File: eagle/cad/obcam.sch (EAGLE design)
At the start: 15 parts, among them IC1 NJM2391, IC2 TJ8S06M3L

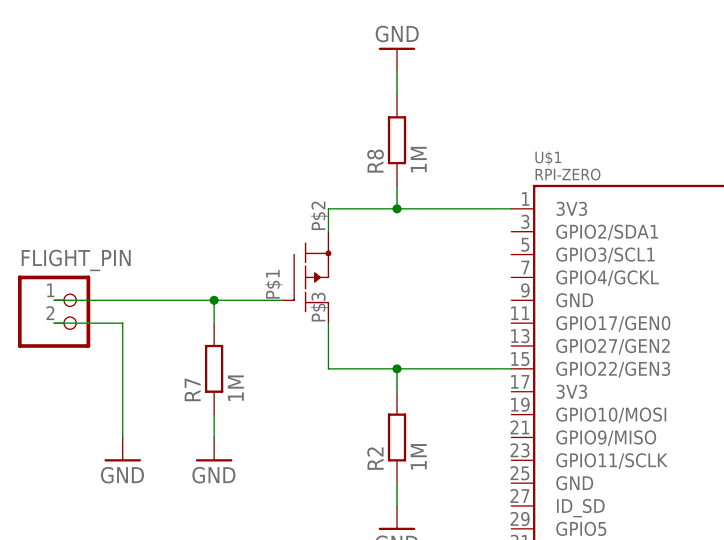
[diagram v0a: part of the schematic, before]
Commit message: Fixed the library of TJ8S06M3L and updated CAD.
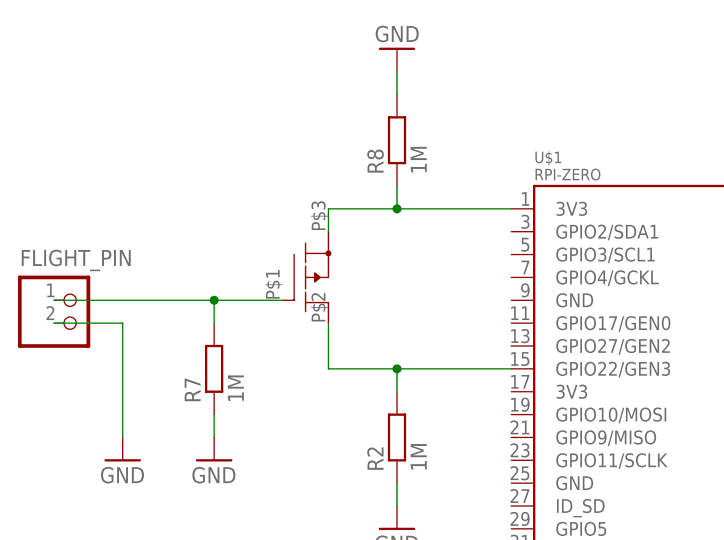
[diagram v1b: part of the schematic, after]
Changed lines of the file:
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@@
 <part name="IC1" library="2022_nse" deviceset="NJM2391" device=""/>
 <part name="D1" library="2022_nse" deviceset="SML-E1X" device=""/>
-<part name="IC2" library="2022_nse" deviceset="TJ8S06M3L" device=""/>
 <part name="R5" library="rcl" library_urn="urn:adsk.eagle:library:334" deviceset="R-EU_" device="M2012" package3d_urn="urn:adsk.eagle:package:23561/2" value="1k"/>
 <part name="R6" library="rcl" library_urn="urn:adsk.eagle:library:334" deviceset="R-EU_" device="M2012" package3d_urn="urn:adsk.eagle:package:23561/2" value="10k"/>
@@
 <part name="R8" library="rcl" library_urn="urn:adsk.eagle:library:334" deviceset="R-EU_" device="M2012" package3d_urn="urn:adsk.eagle:package:23561/2" value="1M"/>
 <part name="GND10" library="supply1" library_urn="urn:adsk.eagle:library:371" deviceset="GND" device=""/>
+<part name="IC2" library="2022_nse" deviceset="TJ8S06M3L" device=""/>
 </parts>
 <sheets>
@@
 <instance part="IC1" gate="G$1" x="66.04" y="30.48" smashed="yes"/>
 <instance part="D1" gate="G$1" x="127" y="60.96" smashed="yes"/>
-<instance part="IC2" gate="G$1" x="30.48" y="91.44" smashed="yes" rot="R270"/>
 <instance part="R5" gate="G$1" x="139.7" y="60.96" smashed="yes">
 <attribute name="NAME" x="135.89" y="62.4586" size="1.778" layer="95"/>
@@
 <attribute name="VALUE" x="43.18" y="119.38" size="1.778" layer="96" rot="R180"/>
 </instance>
+<instance part="IC2" gate="G$1" x="30.48" y="91.44" smashed="yes" rot="R270"/>
 </instances>
 <busses>
@@
 <wire x1="2.54" y1="88.9" x2="20.32" y2="88.9" width="0.1524" layer="91"/>
 <wire x1="20.32" y1="88.9" x2="27.94" y2="88.9" width="0.1524" layer="91"/>
-<pinref part="IC2" gate="G$1" pin="P$1"/>
 <pinref part="R7" gate="G$1" pin="2"/>
 <wire x1="20.32" y1="86.36" x2="20.32" y2="88.9" width="0.1524" layer="91"/>
 <junction x="20.32" y="88.9"/>
+<pinref part="IC2" gate="G$1" pin="P$1"/>
 </segment>
 </net>
@@
 <wire x1="40.64" y1="81.28" x2="53.34" y2="81.28" width="0.1524" layer="91"/>
 <junction x="40.64" y="81.28"/>
-<pinref part="IC2" gate="G$1" pin="P$3"/>
 <wire x1="33.02" y1="86.36" x2="33.02" y2="81.28" width="0.1524" layer="91"/>
 <wire x1="33.02" y1="81.28" x2="40.64" y2="81.28" width="0.1524" layer="91"/>
+<pinref part="IC2" gate="G$1" pin="P$3"/>
 </segment>
 </net>
@@
 <net name="3V3@1" class="0">
 <segment>
-<pinref part="IC2" gate="G$1" pin="P$2"/>
 <pinref part="U$1" gate="G$1" pin="3V3@1"/>
 <wire x1="33.02" y1="96.52" x2="33.02" y2="99.06" width="0.1524" layer="91"/>
@@
 <wire x1="40.64" y1="99.06" x2="40.64" y2="101.6" width="0.1524" layer="91"/>
 <junction x="40.64" y="99.06"/>
-</segment>
-</net>
+<pinref part="IC2" gate="G$1" pin="P$2"/>
+</segment>
+</net>
